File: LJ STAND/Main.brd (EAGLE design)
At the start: 180 x 152 mm, 210 parts, among them Q1 200mA/50V

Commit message: Light PCB routing
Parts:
- removed C14, C15: 22nF, SparkFun-Capacitors:0805
- removed R43, R44: 1K, SparkFun-Resistors:0603-RES
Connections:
- removed net N$27: IR_1.1, R44.2
- removed net N$46: IR_0.1, R43.2
- net GND: no longer C14.2, C15.2
- net IR_0: now also IR_0.1; no longer C14.1, R43.1
- net IR_1: now also IR_1.1; no longer C15.1, R44.1

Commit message: Finished routing light & encoder pcbs
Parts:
- removed C16, C17, C18, C19, C20, C21, C22, C23, C24, C25, C26, C27, C28, C29, C30, C31, C32, C33, C34, C35, C36, C37: 22nF, SparkFun-Capacitors:0805
- removed R45, R46, R47, R48, R49, R50, R51, R52, R53, R54, R55, R56, R57, R58, R59, R60, R61, R62, R63, R64, R65, R66: 1K, SparkFun-Resistors:0603-RES
- added LS_CONNECTOR: (no value), pinhead+:2X08_SMT
- renumbered IR_0 to IR0, IR_1 to IR1, IR_10 to IR10, IR_11 to IR11, IR_12 to IR12, IR_13 to IR13, IR_14 to IR14, IR_15 to IR15, IR_16 to IR16, IR_17 to IR17, IR_18 to IR18, IR_19 to IR19, IR_2 to IR2, IR_20 to IR20, IR_21 to IR21, IR_22 to IR22, IR_23 to IR23, IR_3 to IR3, IR_4 to IR4, IR_5 to IR5, IR_6 to IR6, IR_7 to IR7, IR_8 to IR8, IR_9 to IR9
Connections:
- net IR_0 renamed IR0
- net IR_1 renamed IR1
- removed net IR_10: C24.1, R53.1, SLAVE_SENSOR.19
- removed net IR_11: C25.1, R54.1, SLAVE_SENSOR.20
- removed net IR_12: C26.1, R55.1, SLAVE_SENSOR.21
- removed net IR_13: C27.1, R56.1, SLAVE_SENSOR.22
- removed net IR_14: C28.1, R57.1, SLAVE_SENSOR.23
- removed net IR_15: C29.1, R58.1, SLAVE_SENSOR.24
- removed net IR_16: C30.1, R59.1, SLAVE_SENSOR.25
- removed net IR_17: C31.1, R60.1, SLAVE_SENSOR.26
- removed net IR_18: C32.1, R61.1, SLAVE_SENSOR.27
- removed net IR_19: C33.1, R62.1, SLAVE_SENSOR.28
- removed net IR_2: C16.1, R45.1, SLAVE_SENSOR.2
- removed net IR_20: C34.1, R63.1, SLAVE_SENSOR.29
- removed net IR_21: C35.1, R64.1, SLAVE_SENSOR.30
- removed net IR_22: C36.1, R65.1, SLAVE_SENSOR.31
- removed net IR_23: C37.1, R66.1, SLAVE_SENSOR.32
- removed net IR_3: C17.1, R46.1, SLAVE_SENSOR.3
- removed net IR_4: C18.1, R47.1, SLAVE_SENSOR.4
- removed net IR_5: C19.1, R48.1, SLAVE_SENSOR.5
- removed net IR_6: C20.1, R49.1, SLAVE_SENSOR.6
- removed net IR_7: C21.1, R50.1, SLAVE_SENSOR.7
- removed net IR_8: C22.1, R51.1, SLAVE_SENSOR.8
- removed net IR_9: C23.1, R52.1, SLAVE_SENSOR.9
- removed net LS_0: SLAVE_SENSOR.14
- removed net LS_1: SLAVE_SENSOR.15
- removed net LS_2: SLAVE_SENSOR.16
- removed net LS_3: SLAVE_SENSOR.17
- removed net N$47: IR2.1, R45.2
- removed net N$48: IR3.1, R46.2
- removed net N$49: IR4.1, R47.2
- removed net N$50: IR5.1, R48.2
- removed net N$51: IR6.1, R49.2
- removed net N$52: IR7.1, R50.2
- removed net N$53: IR8.1, R51.2
- removed net N$54: IR9.1, R52.2
- removed net N$55: IR10.1, R53.2
- removed net N$56: IR11.1, R54.2
- removed net N$57: IR12.1, R55.2
- removed net N$58: IR13.1, R56.2
- removed net N$59: IR14.1, R57.2
- removed net N$60: IR15.1, R58.2
- removed net N$61: IR16.1, R59.2
- removed net N$62: IR17.1, R60.2
- removed net N$63: IR18.1, R61.2
- removed net N$64: IR19.1, R62.2
- removed net N$65: IR20.1, R63.2
- removed net N$66: IR21.1, R64.2
- removed net N$67: IR22.1, R65.2
- removed net N$68: IR23.1, R66.2
- new net IR10: IR10.1, SLAVE_SENSOR.19
- new net IR11: IR11.1, SLAVE_SENSOR.20
- new net IR12: IR12.1, SLAVE_SENSOR.21
- new net IR13: IR13.1, SLAVE_SENSOR.22
- new net IR14: IR14.1, SLAVE_SENSOR.23
- new net IR15: IR15.1, SLAVE_SENSOR.24
- new net IR16: IR16.1, SLAVE_SENSOR.25
- new net IR17: IR17.1, SLAVE_SENSOR.26
- new net IR18: IR18.1, SLAVE_SENSOR.27
- new net IR19: IR19.1, SLAVE_SENSOR.28
- new net IR2: IR2.1, SLAVE_SENSOR.2
- new net IR20: IR20.1, SLAVE_SENSOR.29
- new net IR21: IR21.1, SLAVE_SENSOR.30
- new net IR22: IR22.1, SLAVE_SENSOR.31
- new net IR23: IR23.1, SLAVE_SENSOR.32
- new net IR3: IR3.1, SLAVE_SENSOR.3
- new net IR4: IR4.1, SLAVE_SENSOR.4
- new net IR5: IR5.1, SLAVE_SENSOR.5
- new net IR6: IR6.1, SLAVE_SENSOR.6
- new net IR7: IR7.1, SLAVE_SENSOR.7
- new net IR8: IR8.1, SLAVE_SENSOR.8
- new net IR9: IR9.1, SLAVE_SENSOR.9
- new net IR_PWR: C38.1, C39.1, C40.1, C41.1, C42.1, C43.1, C44.1, C45.1, C46.1, C47.1, C48.1, C49.1, C50.1, C51.1, C52.1, C53.1, C54.1, C55.1, C56.1, C57.1, C58.1, C59.1, C60.1, C61.1, IR0.3, IR1.3, IR10.3, IR11.3, IR12.3, IR13.3, IR14.3, IR15.3, IR16.3, IR17.3, IR18.3, IR19.3, IR2.3, IR20.3, IR21.3, IR22.3, IR23.3, IR3.3, IR4.3, IR5.3, IR6.3, IR7.3, IR8.3, IR9.3, SLAVE_SENSOR.43, SLAVE_SENSOR.44, SLAVE_SENSOR.45
- new net LS0: LS_CONNECTOR.7, SLAVE_SENSOR.14
- new net LS1: LS_CONNECTOR.5, SLAVE_SENSOR.15
- new net LS2: LS_CONNECTOR.3, SLAVE_SENSOR.16
- new net LS3: LS_CONNECTOR.1, SLAVE_SENSOR.17
- new net MUX_A0: LS_CONNECTOR.4, SLAVE_SENSOR.33
- new net MUX_A1: LS_CONNECTOR.2, SLAVE_SENSOR.34
- new net MUX_A2: LS_CONNECTOR.6, SLAVE_SENSOR.35
- new net MUX_A3: LS_CONNECTOR.8, SLAVE_SENSOR.36
- new net MUX_A4: LS_CONNECTOR.10, SLAVE_SENSOR.37
- new net MUX_CS: LS_CONNECTOR.12, SLAVE_SENSOR.38
- new net MUX_EN: LS_CONNECTOR.16, SLAVE_SENSOR.46
- new net MUX_WR: LS_CONNECTOR.14, SLAVE_SENSOR.39
- net 3.3V: now also LS_CONNECTOR.9; no longer C38.1, C39.1, C40.1, C41.1, C42.1, C43.1, C44.1, C45.1, C46.1, C47.1, C48.1, C49.1, C50.1, C51.1, C52.1, C53.1, C54.1, C55.1, C56.1, C57.1, C58.1, C59.1, C60.1, C61.1, IR0.3, IR1.3, IR10.3, IR11.3, IR12.3, IR13.3, IR14.3, IR15.3, IR16.3, IR17.3, IR18.3, IR19.3, IR2.3, IR20.3, IR21.3, IR22.3, IR23.3, IR3.3, IR4.3, IR5.3, IR6.3, IR7.3, IR8.3, IR9.3
- net GND: now also LS_CONNECTOR.11, LS_CONNECTOR.13; no longer C16.2, C17.2, C18.2, C19.2, C20.2, C21.2, C22.2, C23.2, C24.2, C25.2, C26.2, C27.2, C28.2, C29.2, C30.2, C31.2, C32.2, C33.2, C34.2, C35.2, C36.2, C37.2
- net LS_MUX: now also LS_CONNECTOR.15

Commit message: Main PCB routing
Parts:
- added C14, C15, C16, C17: 0.1uF, SparkFun-Capacitors:0805
- added LEDA1, LEDA2, LEDA3, LEDA4, LEDA5, LEDA6, LED_DEBUG1: RED, SparkFun-LED:LED-0603
- added LEDD1, LEDD2, LEDD3, LEDD4, LEDD5, LEDD6, LED_DEBUG6: WHITE, SparkFun-LED:LED-0603
- added LED_DEBUG2: GREEN, SparkFun-LED:LED-0603
- added LED_DEBUG3: BLUE, SparkFun-LED:LED-0603
- added LED_DEBUG4: ORANGE, SparkFun-LED:LED-0603
- added LED_DEBUG5: YELLOW, SparkFun-LED:LED-0603
- added LIGHT_GATE: (no value), jst-ph:B5B-PH-K-S
- added LOGIC_SWITCH, MOTOR_SWITCH: (no value), jst-vh:B2P-VH
- added Q2, Q3: (no value), SparkFun-DiscreteSemi:SOT23-3
- added R43, R44, R45, R46, R47, R48, R49, R50, R51, R52, R53, R54, R55, R56, R57, R58, R59, R60: 330, SparkFun-Resistors:0603-RES
- added R61, R62: 1K, SparkFun-Resistors:0603-RES
- added U$2: GYRO, Gyro:GYRO
- 3.3V_ON, 5V_ON: value (none) -> GREEN
- C2, C4, C5: value (none) -> 10uF
- C3: value (none) -> 22uF
- moved C65 575.7 mm to (127.8, 143.3), turned to 270 degrees
- moved C66 573.3 mm to (95.7, 147.6)
- moved C63 569.0 mm to (165.5, 127.0), turned to 300 degrees
- moved C64 567.0 mm to (61.5, 147.9)
- moved R67 565.2 mm to (48.9, 141.0), turned to 270 degrees
- moved C62 551.8 mm to (20.1, 137.0), turned to 60 degrees
- moved C68 536.6 mm to (174.2, 84.1), turned to 270 degrees
- moved C67 510.7 mm to (5.77, 95.9), turned to 90 degrees
- moved C70 495.2 mm to (159.8, 42.9), turned to 240 degrees
- moved C73 470.4 mm to (14.3, 53.2), turned to 120 degrees
- moved C69 455.5 mm to (126.8, 14.2), turned to 210 degrees
- moved C72 441.5 mm to (43.0, 20.2), turned to 150 degrees
- moved C71 436.3 mm to (84.3, 5.94), turned to 180 degrees
- moved R40 273.7 mm to (105.1, 48.3), flipped to the bottom, turned to 270 degrees
- moved R36 273.3 mm to (110.2, 51.0), flipped to the bottom
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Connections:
- removed net CAM_SCL: U$1.15
- removed net CAM_SDA: U$1.16
- new net CAM_RX: MASTER.7, U$1.15
- new net CAM_TX: MASTER.8, U$1.16
- new net GYRO_CS1: MASTER.43, U$2.CS1
- new net GYRO_CS2: MASTER.42, U$2.CS2
- new net GYRO_CS3: MASTER.54, U$2.CS3
- new net GYRO_MISO: MASTER.45, U$2.MISO
- new net GYRO_MOSI: MASTER.44, U$2.MOSI
- new net GYRO_SCLK: MASTER.46, U$2.SCLK
- new net LED_A_CTRL: R61.1, SLAVE_DEBUG.2
- new net LED_DEBUG1: R55.1, SLAVE_DEBUG.4
- new net LED_DEBUG2: R56.1, SLAVE_DEBUG.5
- new net LED_DEBUG3: R57.1, SLAVE_DEBUG.6
- new net LED_DEBUG4: R58.1, SLAVE_DEBUG.7
- new net LED_DEBUG5: R59.1, SLAVE_DEBUG.8
- new net LED_DEBUG6: R60.1, SLAVE_DEBUG.9
- new net LED_D_CTRL: R62.1, SLAVE_DEBUG.3
- new net LIGHT_GATE_LASER: LIGHT_GATE.3
- new net LIGHT_GATE_OUT: LIGHT_GATE.2
- new net N$1: MOTOR_FUSE.1, MOTOR_FUSE.2, MOTOR_SWITCH.2
- new net N$10: LEDA1.C, LEDA2.C, LEDA3.C, LEDA4.C, LEDA5.C, LEDA6.C, Q2.3
- new net N$2: LOGIC_FUSE.1, LOGIC_FUSE.2, LOGIC_SWITCH.1
- new net N$27: LEDD1.A, R49.2
- new net N$3: LEDA1.A, R43.2
- new net N$4: LEDA2.A, R44.2
- new net N$46: LEDD2.A, R50.2
- new net N$47: LEDD3.A, R51.2
- new net N$48: LEDD4.A, R52.2
- new net N$49: LEDD5.A, R53.2
- new net N$5: LEDA3.A, R45.2
- new net N$50: LEDD6.A, R54.2
- new net N$51: LEDD1.C, LEDD2.C, LEDD3.C, LEDD4.C, LEDD5.C, LEDD6.C, Q3.3
- new net N$52: LED_DEBUG1.A, R55.2
- new net N$53: LED_DEBUG2.A, R56.2
- new net N$54: LED_DEBUG3.A, R57.2
- new net N$55: LED_DEBUG4.A, R58.2
- new net N$56: LED_DEBUG5.A, R59.2
- new net N$57: LED_DEBUG6.A, R60.2
- new net N$58: Q2.1, R61.2
- new net N$59: Q3.1, R62.2
- new net N$6: LEDA4.A, R46.2
- new net N$61: LIGHT_GATE.4
- new net N$8: LEDA5.A, R47.2
- new net N$9: LEDA6.A, R48.2
- net 3.3V: now also C14.1, C15.1, C16.1, C17.1, LIGHT_GATE.1, MASTER.3.3V-1, R43.1, R44.1, R45.1, R46.1, R47.1, R48.1, R49.1, R50.1, R51.1, R52.1, R53.1, R54.1, SLAVE_DEBUG.3.3V-1, SLAVE_MOTOR.3.3V-1, SLAVE_SENSOR.3.3V-1, U$2.3.3V
- net GND: now also C14.2, C15.2, C16.2, C17.2, LED_DEBUG1.C, LED_DEBUG2.C, LED_DEBUG3.C, LED_DEBUG4.C, LED_DEBUG5.C, LED_DEBUG6.C, LIGHT_GATE.5, MASTER.AGND, MASTER.GND-1, MASTER.GND-2, MASTER.GND-3, MASTER.GND-4, Q2.2, Q3.2, SLAVE_DEBUG.AGND, SLAVE_DEBUG.GND, SLAVE_DEBUG.GND-1, SLAVE_DEBUG.GND-2, SLAVE_DEBUG.GND-3, SLAVE_DEBUG.GND-4, SLAVE_MOTOR.AGND, SLAVE_MOTOR.GND, SLAVE_MOTOR.GND-1, SLAVE_MOTOR.GND-2, SLAVE_MOTOR.GND-3, SLAVE_MOTOR.GND-4, SLAVE_SENSOR.AGND, SLAVE_SENSOR.GND, SLAVE_SENSOR.GND-1, SLAVE_SENSOR.GND-2, SLAVE_SENSOR.GND-3, SLAVE_SENSOR.GND-4, U$2.GND
- net N$12: now also LOGIC_SWITCH.2, MOTOR_SWITCH.1; no longer LOGIC_FUSE.1, LOGIC_FUSE.2, MOTOR_FUSE.1, MOTOR_FUSE.2
- net RGB_LED_DATA: now also SLAVE_DEBUG.23
- net SCREEN_C/D: now also SLAVE_DEBUG.21
- net SCREEN_CS: now also SLAVE_DEBUG.22
- net SCREEN_D0: now also SLAVE_DEBUG.24
- net SCREEN_D1: now also SLAVE_DEBUG.25
- net SCREEN_D2: now also SLAVE_DEBUG.26
- net SCREEN_D3: now also SLAVE_DEBUG.27
- net SCREEN_D4: now also SLAVE_DEBUG.28
- net SCREEN_D5: now also SLAVE_DEBUG.29
- net SCREEN_D6: now also SLAVE_DEBUG.30
- net SCREEN_D7: now also SLAVE_DEBUG.31
- net SCREEN_RD: now also SLAVE_DEBUG.19
- net SCREEN_WR: now also SLAVE_DEBUG.20
- net SCREEN_X+: now also SLAVE_DEBUG.15
- net SCREEN_X-: now also SLAVE_DEBUG.16
- net SCREEN_Y+: now also SLAVE_DEBUG.17
- net SCREEN_Y-: now also SLAVE_DEBUG.18
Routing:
- net 5V: track 0.00 -> 620.4 mm, vias 0 -> 2
- net IR_PWR: track 0.00 -> 609.9 mm, vias 0 -> 2
- net N$51: track 0.00 -> 566.2 mm, vias 0 -> 7
- net N$10: track 0.00 -> 542.8 mm, vias 0 -> 6
- net IR18: track 0.00 -> 326.1 mm, vias 0 -> 2
- net IR19: track 0.00 -> 300.6 mm, vias 0 -> 2
- net IR17: track 0.00 -> 300.4 mm, vias 0 -> 3
- net IR20: track 0.00 -> 278.5 mm, vias 0 -> 2
- net IR16: track 0.00 -> 277.0 mm, vias 0 -> 3
- net MOSI: track 0.00 -> 259.0 mm, vias 0 -> 5
- net IR21: track 0.00 -> 258.4 mm, vias 0 -> 3
- net MISO: track 0.00 -> 255.4 mm, vias 0 -> 5
- net IR15: track 0.00 -> 254.9 mm, vias 0 -> 3
- net SCK: track 0.00 -> 247.1 mm, vias 0 -> 2
- net IR22: track 0.00 -> 236.3 mm, vias 0 -> 2
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- added copper zone on layer 1, net GND
- added copper zone on layer 16, net GND
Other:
- outline, holes or cut-outs redrawn

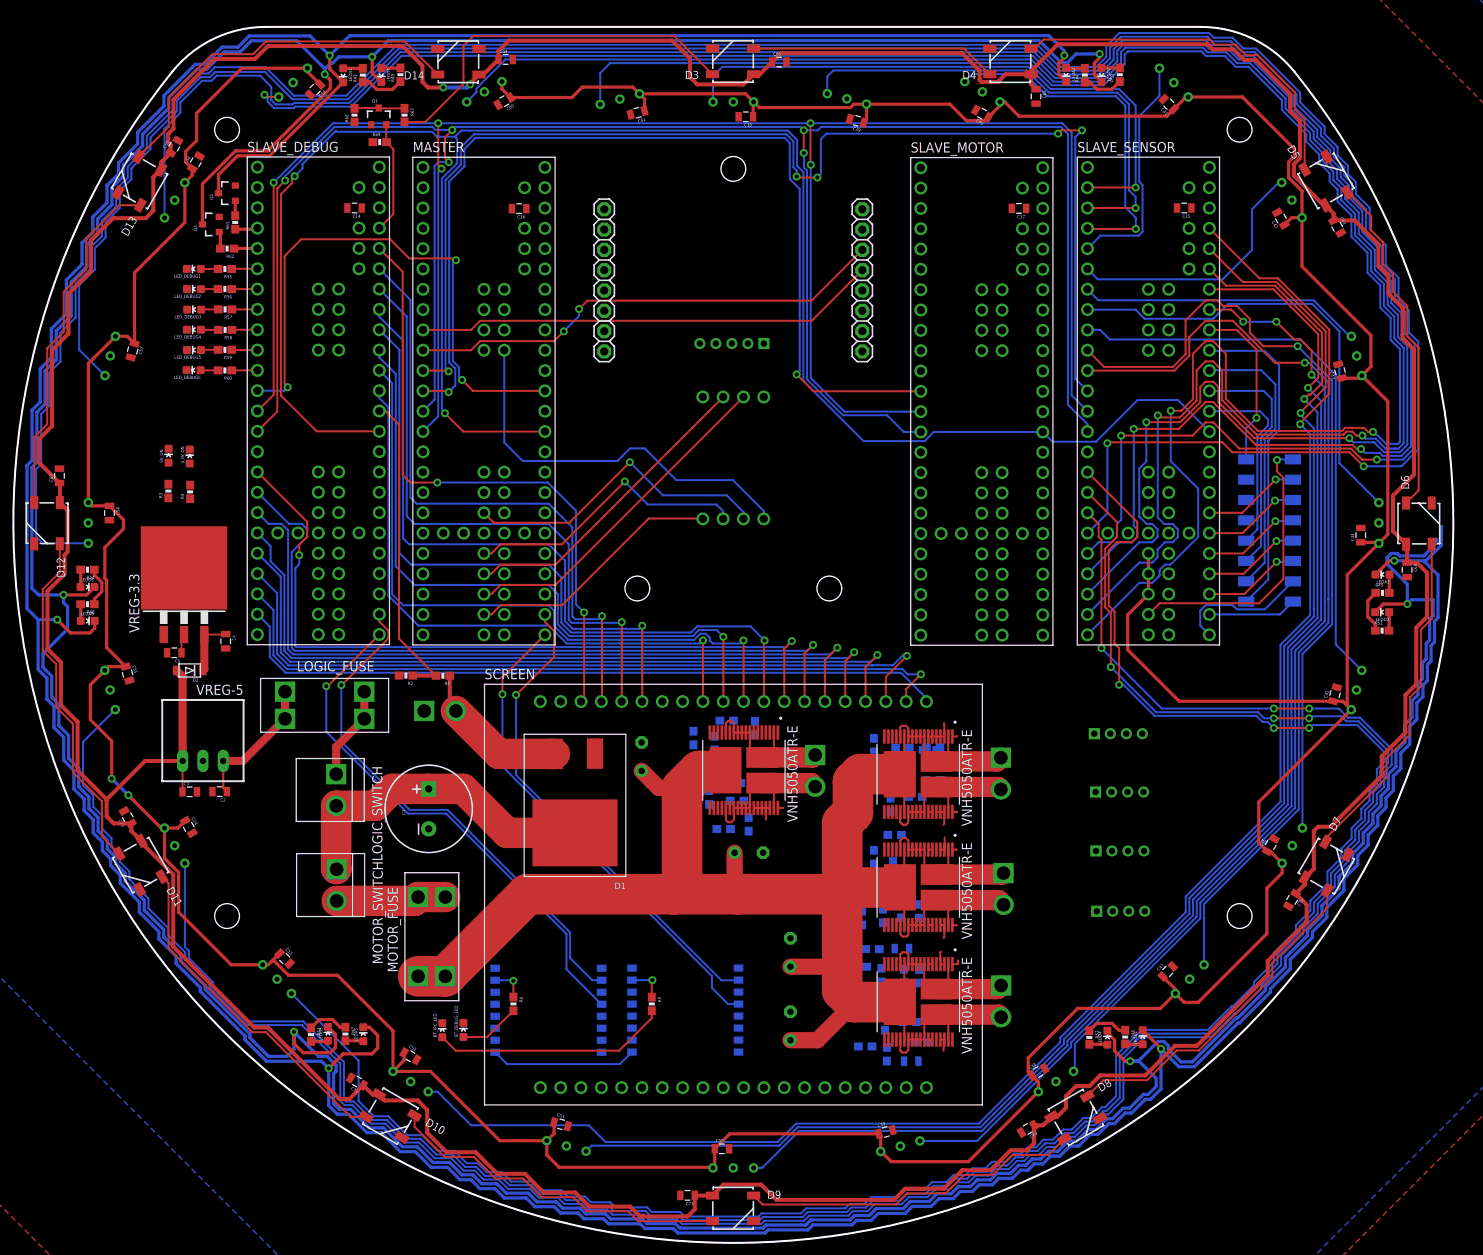
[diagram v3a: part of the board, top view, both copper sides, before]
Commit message: Finished routing main pcb
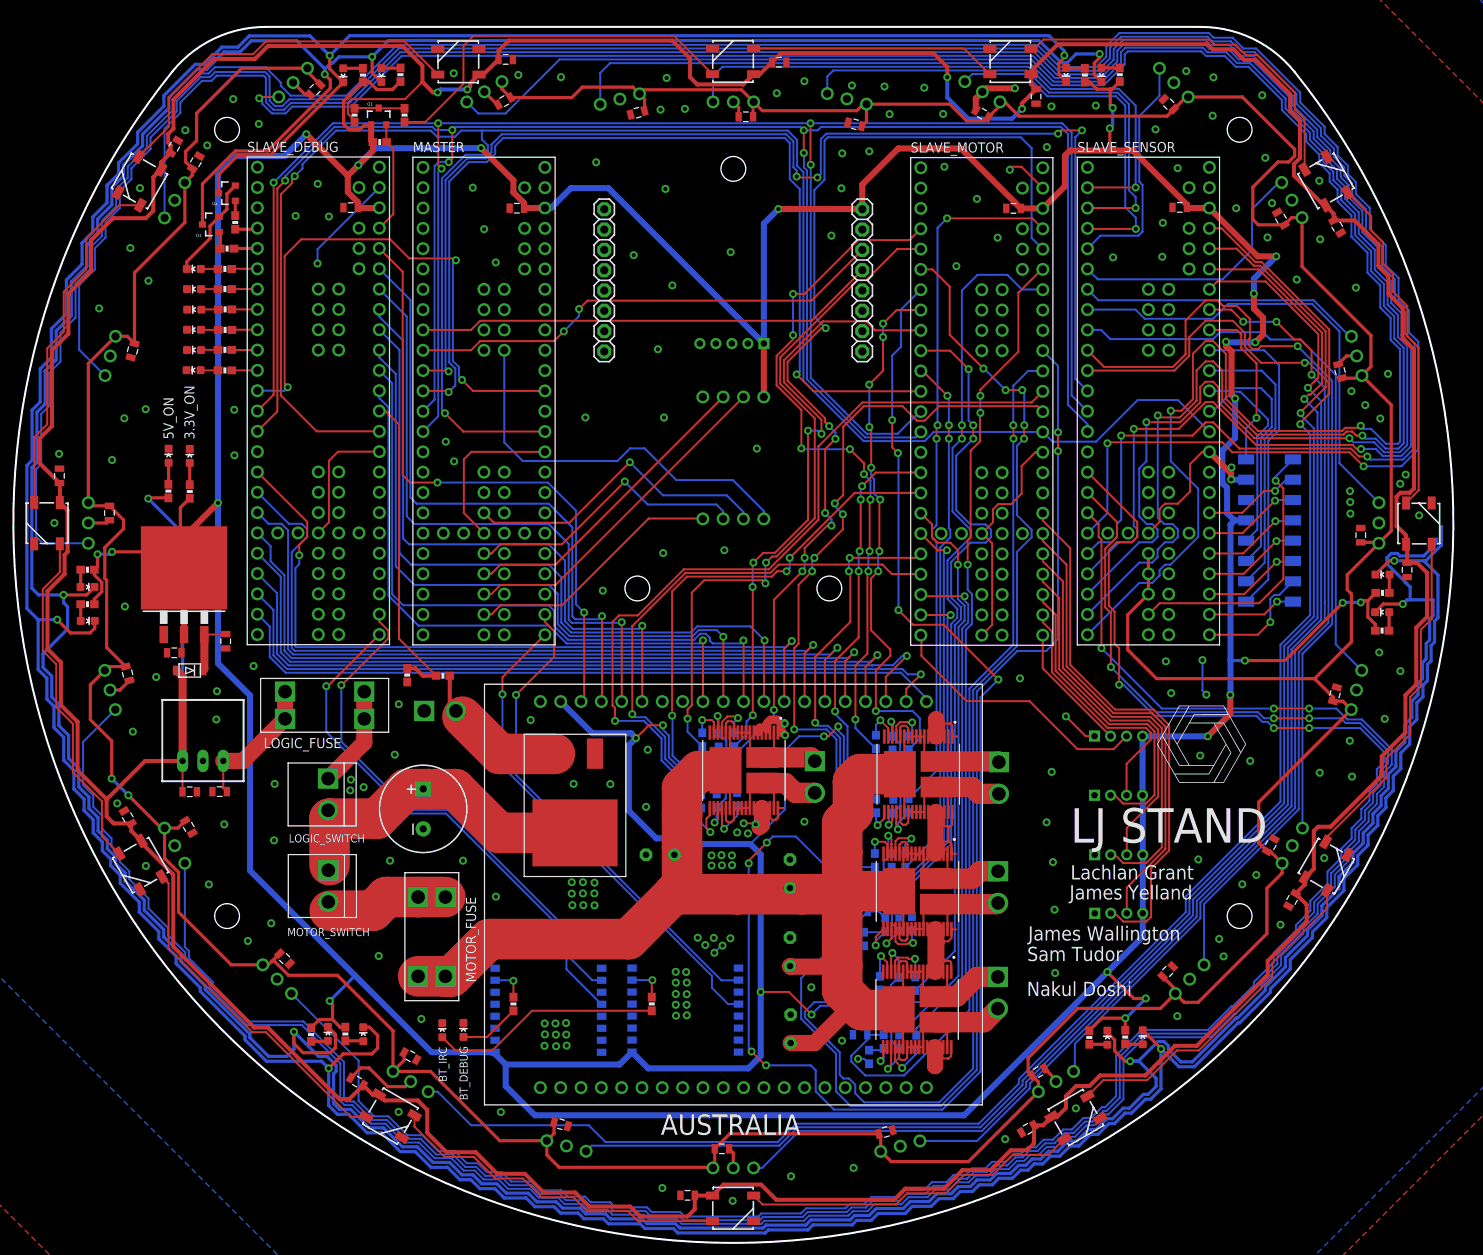
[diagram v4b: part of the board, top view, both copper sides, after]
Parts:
- moved ENC_BR 15.2 mm to (138.2, 41.2)
- moved ENC_BL 15.1 mm to (138.2, 48.5)
- moved ENC_R 14.5 mm to (138.2, 56.0)
- moved ENC_L 14.4 mm to (138.2, 63.3)
- moved C7 12.5 mm to (80.8, 48.5), turned to 0 degrees
- moved C6 9.62 mm to (103.1, 49.6), turned to 270 degrees
- moved R24 7.51 mm to (83.0, 54.4), turned to 0 degrees
- moved C12 7.19 mm to (105.8, 26.0), turned to 0 degrees
- moved C13 6.93 mm to (105.9, 41.4), turned to 0 degrees
- moved R15 6.61 mm to (105.5, 49.6), turned to 270 degrees
- moved R31 6.41 mm to (110.0, 29.6)
- moved R12 5.98 mm to (110.0, 54.6), turned to 90 degrees
- moved C10 5.77 mm to (97.1, 46.1), turned to 90 degrees
- moved C11 5.35 mm to (82.9, 56.6), turned to 0 degrees
- moved R10 5.10 mm to (109.9, 62.5), turned to 270 degrees
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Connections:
- removed net CAM_CS: U$1.14
- removed net CAM_MISO: U$1.12
- removed net CAM_MOSI: U$1.11
- removed net CAM_SCK: U$1.13
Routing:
- net 3.3V: track 52.4 -> 851.4 mm, vias 0 -> 29
- net GND: track 24.6 -> 251.8 mm, vias 0 -> 202
- net MOTOR4_PWM: track 0.00 -> 185.6 mm, vias 0 -> 8
- net MOTOR3_PWM: track 0.00 -> 152.2 mm, vias 0 -> 5
- net MOTOR4_CS: track 0.00 -> 147.5 mm, vias 0 -> 2
- net MOTOR2_INB: track 0.00 -> 133.3 mm, vias 0 -> 8
- net MOTOR3_CS: track 0.00 -> 109.9 mm, vias 0 -> 2
- net MOTOR3_INB: track 0.00 -> 102.8 mm, vias 0 -> 3
- net MOTOR2_CS: track 0.00 -> 100.3 mm, vias 0 -> 1
- net MOTOR4_INB: track 0.00 -> 95.4 mm, vias 0 -> 2
- net MOTOR3_INA: track 0.00 -> 94.7 mm, vias 0 -> 3
- net MOTOR1_CS: track 0.00 -> 92.8 mm, vias 0 -> 5
- net MOTOR1_INB: track 0.00 -> 87.5 mm, vias 0 -> 3
- net MOTOR1_PWM: track 0.00 -> 87.3 mm, vias 0 -> 9
- net MOTOR2_PWM: track 0.00 -> 86.3 mm, vias 0 -> 3
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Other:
- board text added: "+"
- board text added: "-"
- board text added: "3.3V"
- board text added: "AUSTRALIA"
- board text added: "BT_DEBUG"
- board text added: "BT_IRC"
- board text added: "CS1"
- board text added: "CS2"
- board text added: "CS3"
- board text added: "GND"
- board text added: "James Wallington"
- board text added: "James Yelland"
- board text added: "LJ STAND"
- board text added: "Lachlan Grant"
- board text added: "MISO"
- board text added: "MOSI"
- board text added: "Nakul Doshi"
- board text added: "SCKL"
- board text added: "Sam Tudor"
